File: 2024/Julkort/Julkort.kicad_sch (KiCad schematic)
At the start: 28 parts, among them J1 SK-3296S-01-L1, U1 ATtiny44A-M, U2 L78L05_SOT89

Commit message: 2024 v1
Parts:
- removed J1: SK-3296S-01-L1, ProLib_pcs_2024-11-12:SW-SMD_3P-P1.50_L2.7-W6.6, symbol New_Library:SK-3296S-01-L1
- removed U2: L78L05_SOT89, Package_TO_SOT_SMD:SOT-89-3, symbol Regulator_Linear:L78L05_SOT89
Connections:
- net GND: now also USBC1.0 (SH), USBC1.1 (SH), USBC1.2 (SH), USBC1.3 (SH), USBC1.A1 (GND), USBC1.A12 (GND), USBC1.B1 (GND), USBC1.B12 (GND)
- net VCC_REG: now also USBC1.A4 (VBUS), USBC1.A9 (VBUS), USBC1.B4 (VBUS), USBC1.B9 (VBUS)
- no-connect marks 19 -> 15
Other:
- moved on the sheet: TP5

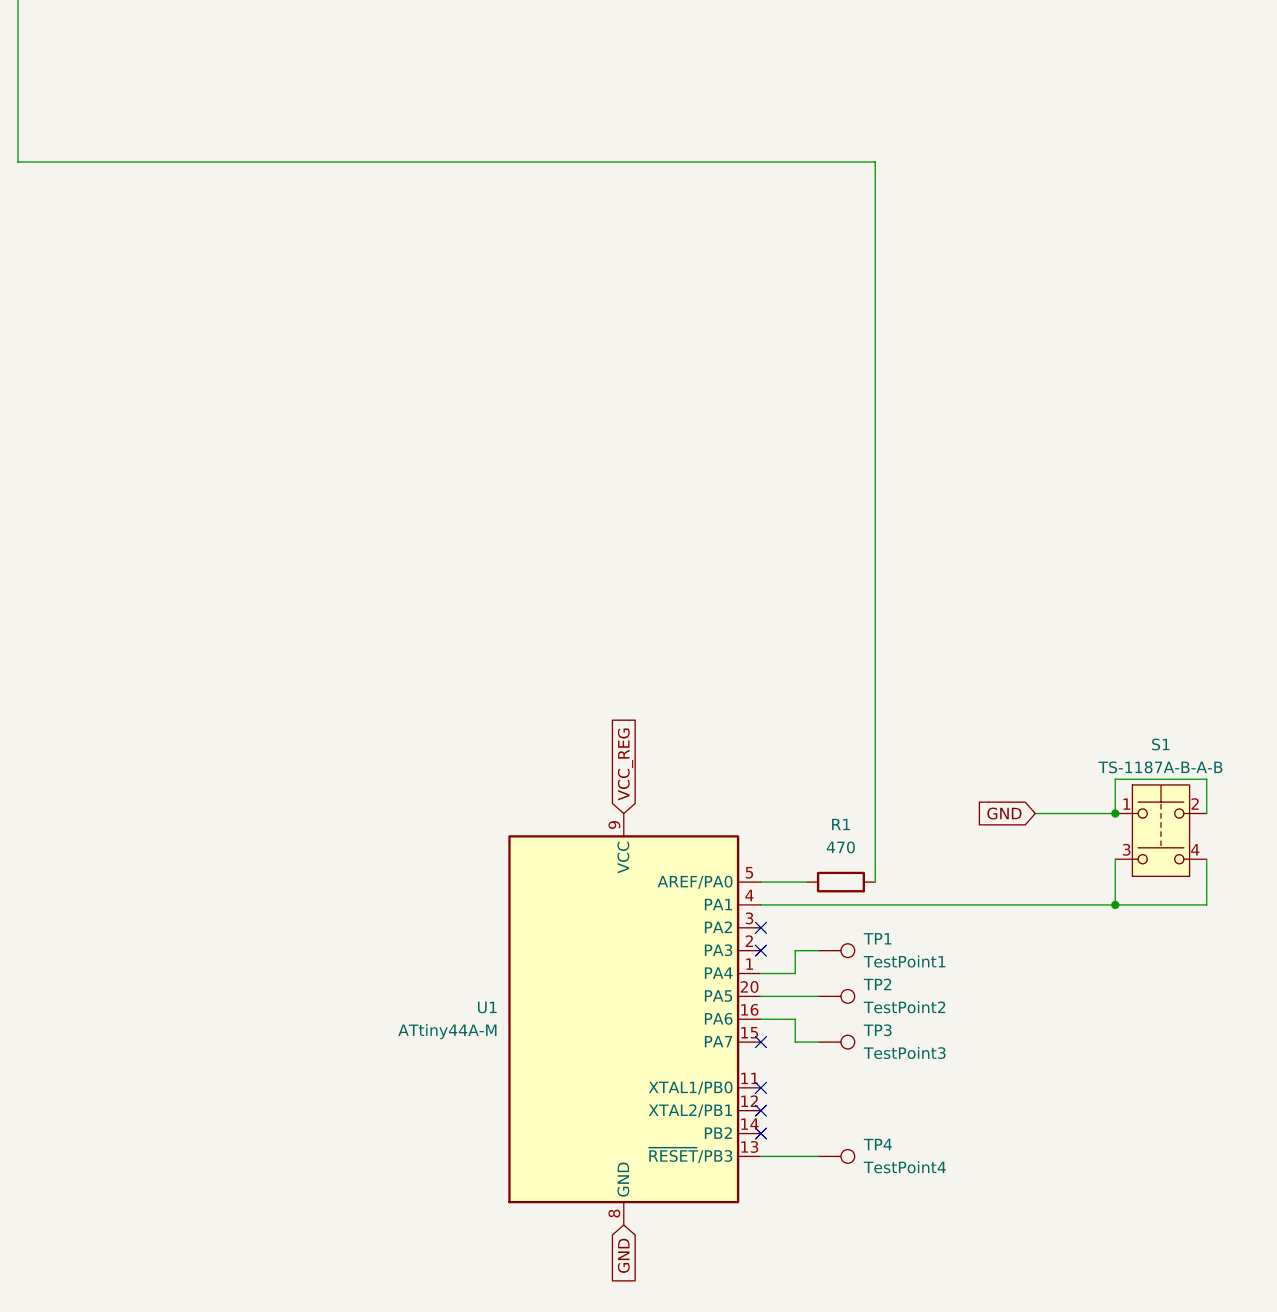
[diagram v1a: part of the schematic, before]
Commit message: Byte av atmega44-footprint
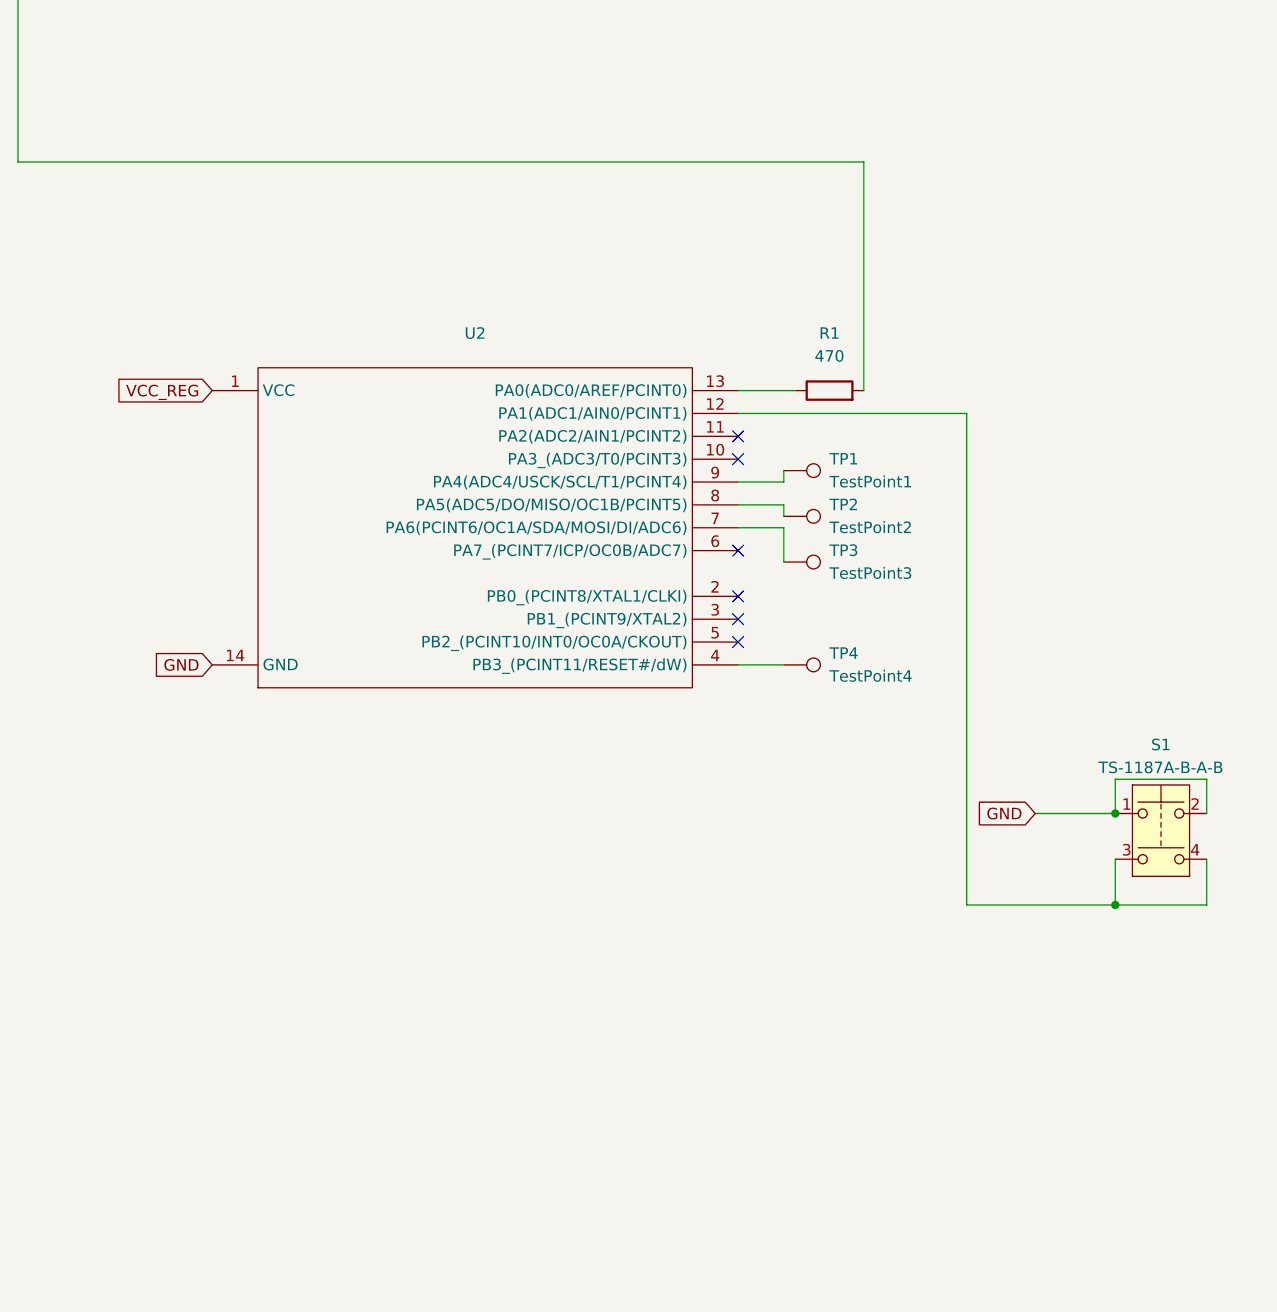
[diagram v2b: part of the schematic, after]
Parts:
- removed U1: ATtiny44A-M, Package_DFN_QFN:QFN-20-1EP_4x4mm_P0.5mm_EP2.5x2.5mm_ThermalVias, symbol MCU_Microchip_ATtiny:ATtiny44A-M
- added U2: ~, footprint:SOP-14_L8.6-W3.9-P1.27-LS6.0-BL, symbol attiny44_new:ATTINY44A-SSUR
- D1, D10, D11, D12, D13, D14, D15, D16, D2, D3, D4, D5, D6, D7, D8, D9: JLCPCB Rotation Offset (none) -> 180; LCSC Part # (none) -> C2909055
- R1: LCSC Part # (none) -> C23179
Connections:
- net GND: now also U2.14 (GND)
- net VCC_REG: now also U2.1 (VCC)
- net at TP1.1: now also U2.9 (PA4(ADC4/USCK/SCL/T1/PCINT4))
- net at S1.3, S1.4: now also U2.12 (PA1(ADC1/AIN0/PCINT1))
- net at TP4.1: now also U2.4 (PB3_(PCINT11/RESET#/dW))
- net at TP3.1: now also U2.7 (PA6(PCINT6/OC1A/SDA/MOSI/DI/ADC6))
- net at TP2.1: now also U2.8 (PA5(ADC5/DO/MISO/OC1B/PCINT5))
- net at R1.1: now also U2.13 (PA0(ADC0/AREF/PCINT0))
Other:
- moved on the sheet: R1
